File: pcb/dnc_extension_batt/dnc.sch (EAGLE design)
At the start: 105 parts, among them Q1 IRF9321PBF, Q2 IRF9321PBF, Q3 BSS138, Q5 BSS138, U1 LCD-16X2NOHOLES, U2 74HCT595D

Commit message: minor change : - logo size - add fuse on led - enclosure
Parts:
- U$2, U$6MOV: value LOGO -> LOGOSIZE2; device pierre_vv:LOGO -> pierre_vv:LOGOSIZE2
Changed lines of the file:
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@@
 <grid distance="0.1" unitdist="inch" unit="inch" style="lines" multiple="1" display="no" altdistance="0.01" altunitdist="inch" altunit="inch"/>
 <layers>
-<layer number="1" name="Top" color="4" fill="1" visible="no" active="no"/>
-<layer number="16" name="Bottom" color="1" fill="1" visible="no" active="no"/>
-<layer number="17" name="Pads" color="2" fill="1" visible="no" active="no"/>
-<layer number="18" name="Vias" color="2" fill="1" visible="no" active="no"/>
-<layer number="19" name="Unrouted" color="13" fill="1" visible="no" active="no"/>
-<layer number="20" name="Dimension" color="15" fill="1" visible="no" active="no"/>
-<layer number="21" name="tPlace" color="7" fill="1" visible="no" active="no"/>
-<layer number="22" name="bPlace" color="7" fill="1" visible="no" active="no"/>
-<layer number="23" name="tOrigins" color="15" fill="1" visible="no" active="no"/>
-<layer number="24" name="bOrigins" color="15" fill="1" visible="no" active="no"/>
-<layer number="25" name="tNames" color="7" fill="1" visible="no" active="no"/>
-<layer number="26" name="bNames" color="7" fill="1" visible="no" active="no"/>
-<layer number="27" name="tValues" color="7" fill="1" visible="no" active="no"/>
-<layer number="28" name="bValues" color="7" fill="1" visible="no" active="no"/>
+<layer number="1" name="Top" color="4" fill="1" visible="yes" active="no"/>
+<layer number="16" name="Bottom" color="1" fill="1" visible="yes" active="no"/>
+<layer number="17" name="Pads" color="2" fill="1" visible="yes" active="no"/>
+<layer number="18" name="Vias" color="2" fill="1" visible="yes" active="no"/>
+<layer number="19" name="Unrouted" color="13" fill="1" visible="yes" active="no"/>
+<layer number="20" name="Dimension" color="15" fill="1" visible="yes" active="no"/>
+<layer number="21" name="tPlace" color="7" fill="1" visible="yes" active="no"/>
+<layer number="22" name="bPlace" color="7" fill="1" visible="yes" active="no"/>
+<layer number="23" name="tOrigins" color="15" fill="1" visible="yes" active="no"/>
+<layer number="24" name="bOrigins" color="15" fill="1" visible="yes" active="no"/>
+<layer number="25" name="tNames" color="7" fill="1" visible="yes" active="no"/>
+<layer number="26" name="bNames" color="7" fill="1" visible="yes" active="no"/>
+<layer number="27" name="tValues" color="7" fill="1" visible="yes" active="no"/>
+<layer number="28" name="bValues" color="7" fill="1" visible="yes" active="no"/>
 <layer number="29" name="tStop" color="7" fill="3" visible="no" active="no"/>
 <layer number="30" name="bStop" color="7" fill="6" visible="no" active="no"/>
@@
 <layer number="35" name="tGlue" color="7" fill="4" visible="no" active="no"/>
 <layer number="36" name="bGlue" color="7" fill="5" visible="no" active="no"/>
-<layer number="37" name="tTest" color="7" fill="1" visible="no" active="no"/>
-<layer number="38" name="bTest" color="7" fill="1" visible="no" active="no"/>
+<layer number="37" name="tTest" color="7" fill="1" visible="yes" active="no"/>
+<layer number="38" name="bTest" color="7" fill="1" visible="yes" active="no"/>
 <layer number="39" name="tKeepout" color="4" fill="11" visible="no" active="no"/>
 <layer number="40" name="bKeepout" color="1" fill="11" visible="no" active="no"/>
@@
 <layer number="44" name="Drills" color="7" fill="1" visible="no" active="no"/>
 <layer number="45" name="Holes" color="7" fill="1" visible="no" active="no"/>
-<layer number="46" name="Milling" color="3" fill="1" visible="no" active="no"/>
-<layer number="47" name="Measures" color="7" fill="1" visible="no" active="no"/>
-<layer number="48" name="Document" color="7" fill="1" visible="no" active="no"/>
-<layer number="49" name="Reference" color="7" fill="1" visible="no" active="no"/>
-<layer number="50" name="dxf" color="7" fill="1" visible="no" active="no"/>
-<layer number="51" name="tDocu" color="14" fill="1" visible="no" active="no"/>
-<layer number="52" name="bDocu" color="14" fill="1" visible="no" active="no"/>
-<layer number="53" name="tGND_GNDA" color="7" fill="9" visible="no" active="no"/>
-<layer number="54" name="bGND_GNDA" color="1" fill="9" visible="no" active="no"/>
-<layer number="56" name="wert" color="7" fill="1" visible="no" active="no"/>
-<layer number="57" name="tCAD" color="7" fill="1" visible="no" active="no"/>
+<layer number="46" name="Milling" color="3" fill="1" visible="yes" active="no"/>
+<layer number="47" name="Measures" color="7" fill="1" visible="yes" active="no"/>
+<layer number="48" name="Document" color="7" fill="1" visible="yes" active="no"/>
+<layer number="49" name="Reference" color="7" fill="1" visible="yes" active="no"/>
+<layer number="50" name="dxf" color="7" fill="1" visible="yes" active="no"/>
+<layer number="51" name="tDocu" color="14" fill="1" visible="yes" active="no"/>
+<layer number="52" name="bDocu" color="14" fill="1" visible="yes" active="no"/>
+<layer number="53" name="tGND_GNDA" color="7" fill="9" visible="yes" active="no"/>
+<layer number="54" name="bGND_GNDA" color="1" fill="9" visible="yes" active="no"/>
+<layer number="56" name="wert" color="7" fill="1" visible="yes" active="no"/>
+<layer number="57" name="tCAD" color="7" fill="1" visible="yes" active="no"/>
 <layer number="90" name="Modules" color="5" fill="1" visible="yes" active="yes"/>
 <layer number="91" name="Nets" color="2" fill="1" visible="yes" active="yes"/>
@@
 </part>
 <part name="GND13" library="SparkFun-Aesthetics" deviceset="GND" device=""/>
-<part name="U$2" library="pierre_vv" deviceset="LOGO" device=""/>
+<part name="U$2" library="pierre_vv" deviceset="LOGO" device="SIZE2" value="LOGOSIZE2"/>
 <part name="GND22" library="SparkFun-Aesthetics" deviceset="GND" device=""/>
 <part name="RAW_IN" library="pierre_vv" deviceset="DNC_IN2" device="PWR" value="SUPPLY">
@@
 </part>
 <part name="U$5" library="pierre_vv" deviceset="BOITIER" device="BOITIER_FARNELLE_479-0020-0"/>
-<part name="U$6MOV" library="pierre_vv" deviceset="LOGO" device=""/>
+<part name="U$6MOV" library="pierre_vv" deviceset="LOGO" device="SIZE2" value="LOGOSIZE2"/>
 <part name="U1" library="SparkFun-Displays" deviceset="LCD-16X2" device="NOHOLES"/>
 <part name="GND6" library="SparkFun-Aesthetics" deviceset="GND" device=""/>

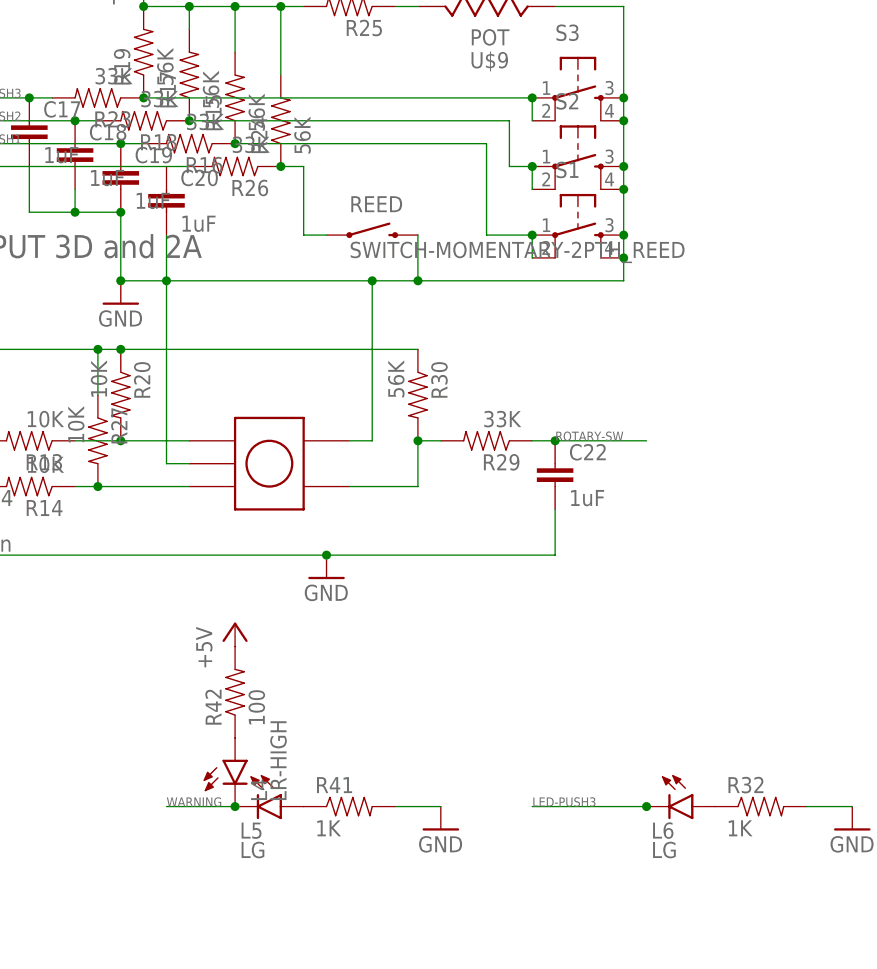
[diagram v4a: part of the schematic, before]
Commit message: change minor : - add rj45 for led string - add select pam led or flex
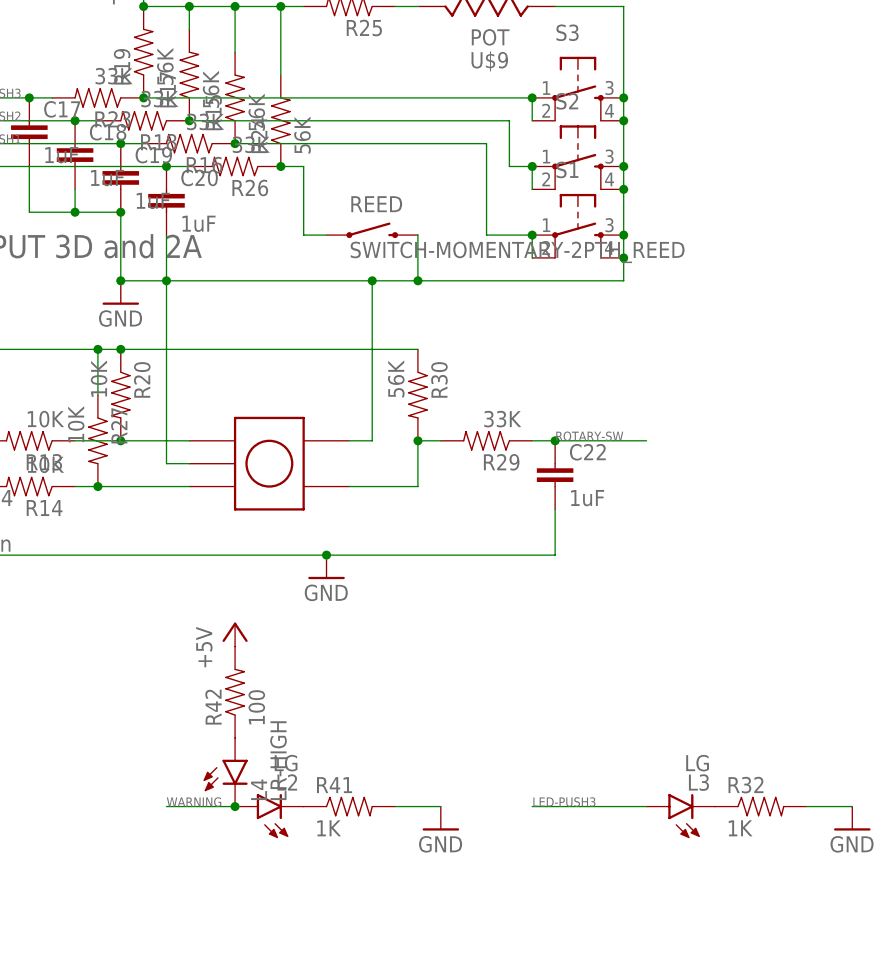
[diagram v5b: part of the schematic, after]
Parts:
- removed L5, L6: LG, SparkFun-LED:LED1206
- added L2, L3: LG, SparkFun-LED:LED1206
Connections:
- net LED-PUSH3: now also L3.A; no longer L6.C
- net N$30: now also L2.C; no longer L5.A
- net N$35: now also L3.C; no longer L6.A
- net WARNING: now also L2.A; no longer L5.C
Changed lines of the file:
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@@
 <grid distance="0.1" unitdist="inch" unit="inch" style="lines" multiple="1" display="no" altdistance="0.01" altunitdist="inch" altunit="inch"/>
 <layers>
-<layer number="1" name="Top" color="4" fill="1" visible="yes" active="no"/>
-<layer number="16" name="Bottom" color="1" fill="1" visible="yes" active="no"/>
-<layer number="17" name="Pads" color="2" fill="1" visible="yes" active="no"/>
-<layer number="18" name="Vias" color="2" fill="1" visible="yes" active="no"/>
-<layer number="19" name="Unrouted" color="13" fill="1" visible="yes" active="no"/>
-<layer number="20" name="Dimension" color="15" fill="1" visible="yes" active="no"/>
-<layer number="21" name="tPlace" color="7" fill="1" visible="yes" active="no"/>
-<layer number="22" name="bPlace" color="7" fill="1" visible="yes" active="no"/>
-<layer number="23" name="tOrigins" color="15" fill="1" visible="yes" active="no"/>
-<layer number="24" name="bOrigins" color="15" fill="1" visible="yes" active="no"/>
-<layer number="25" name="tNames" color="7" fill="1" visible="yes" active="no"/>
-<layer number="26" name="bNames" color="7" fill="1" visible="yes" active="no"/>
-<layer number="27" name="tValues" color="7" fill="1" visible="yes" active="no"/>
-<layer number="28" name="bValues" color="7" fill="1" visible="yes" active="no"/>
+<layer number="1" name="Top" color="4" fill="1" visible="no" active="no"/>
+<layer number="16" name="Bottom" color="1" fill="1" visible="no" active="no"/>
+<layer number="17" name="Pads" color="2" fill="1" visible="no" active="no"/>
+<layer number="18" name="Vias" color="2" fill="1" visible="no" active="no"/>
+<layer number="19" name="Unrouted" color="13" fill="1" visible="no" active="no"/>
+<layer number="20" name="Dimension" color="15" fill="1" visible="no" active="no"/>
+<layer number="21" name="tPlace" color="7" fill="1" visible="no" active="no"/>
+<layer number="22" name="bPlace" color="7" fill="1" visible="no" active="no"/>
+<layer number="23" name="tOrigins" color="15" fill="1" visible="no" active="no"/>
+<layer number="24" name="bOrigins" color="15" fill="1" visible="no" active="no"/>
+<layer number="25" name="tNames" color="7" fill="1" visible="no" active="no"/>
+<layer number="26" name="bNames" color="7" fill="1" visible="no" active="no"/>
+<layer number="27" name="tValues" color="7" fill="1" visible="no" active="no"/>
+<layer number="28" name="bValues" color="7" fill="1" visible="no" active="no"/>
 <layer number="29" name="tStop" color="7" fill="3" visible="no" active="no"/>
 <layer number="30" name="bStop" color="7" fill="6" visible="no" active="no"/>
@@
 <layer number="35" name="tGlue" color="7" fill="4" visible="no" active="no"/>
 <layer number="36" name="bGlue" color="7" fill="5" visible="no" active="no"/>
-<layer number="37" name="tTest" color="7" fill="1" visible="yes" active="no"/>
-<layer number="38" name="bTest" color="7" fill="1" visible="yes" active="no"/>
+<layer number="37" name="tTest" color="7" fill="1" visible="no" active="no"/>
+<layer number="38" name="bTest" color="7" fill="1" visible="no" active="no"/>
 <layer number="39" name="tKeepout" color="4" fill="11" visible="no" active="no"/>
 <layer number="40" name="bKeepout" color="1" fill="11" visible="no" active="no"/>
@@
 <layer number="44" name="Drills" color="7" fill="1" visible="no" active="no"/>
 <layer number="45" name="Holes" color="7" fill="1" visible="no" active="no"/>
-<layer number="46" name="Milling" color="3" fill="1" visible="yes" active="no"/>
-<layer number="47" name="Measures" color="7" fill="1" visible="yes" active="no"/>
-<layer number="48" name="Document" color="7" fill="1" visible="yes" active="no"/>
-<layer number="49" name="Reference" color="7" fill="1" visible="yes" active="no"/>
-<layer number="50" name="dxf" color="7" fill="1" visible="yes" active="no"/>
-<layer number="51" name="tDocu" color="14" fill="1" visible="yes" active="no"/>
-<layer number="52" name="bDocu" color="14" fill="1" visible="yes" active="no"/>
-<layer number="53" name="tGND_GNDA" color="7" fill="9" visible="yes" active="no"/>
-<layer number="54" name="bGND_GNDA" color="1" fill="9" visible="yes" active="no"/>
-<layer number="56" name="wert" color="7" fill="1" visible="yes" active="no"/>
-<layer number="57" name="tCAD" color="7" fill="1" visible="yes" active="no"/>
+<layer number="46" name="Milling" color="3" fill="1" visible="no" active="no"/>
+<layer number="47" name="Measures" color="7" fill="1" visible="no" active="no"/>
+<layer number="48" name="Document" color="7" fill="1" visible="no" active="no"/>
+<layer number="49" name="Reference" color="7" fill="1" visible="no" active="no"/>
+<layer number="50" name="dxf" color="7" fill="1" visible="no" active="no"/>
+<layer number="51" name="tDocu" color="14" fill="1" visible="no" active="no"/>
+<layer number="52" name="bDocu" color="14" fill="1" visible="no" active="no"/>
+<layer number="53" name="tGND_GNDA" color="7" fill="9" visible="no" active="no"/>
+<layer number="54" name="bGND_GNDA" color="1" fill="9" visible="no" active="no"/>
+<layer number="56" name="wert" color="7" fill="1" visible="no" active="no"/>
+<layer number="57" name="tCAD" color="7" fill="1" visible="no" active="no"/>
 <layer number="90" name="Modules" color="5" fill="1" visible="yes" active="yes"/>
 <layer number="91" name="Nets" color="2" fill="1" visible="yes" active="yes"/>
@@
 <part name="R42" library="SparkFun-Passives" deviceset="RESISTOR" device="0603-RES" value="100"/>
 <part name="P+8" library="supply1" deviceset="+5V" device=""/>
-<part name="L5" library="SparkFun-LED" deviceset="LED" device="1206" value="LG"/>
 <part name="R41" library="SparkFun-Passives" deviceset="RESISTOR" device="0603-RES" value="1K"/>
 <part name="GND9" library="SparkFun" deviceset="GND" device=""/>
@@
 <attribute name="P" value="250mw"/>
 </part>
-<part name="L6" library="SparkFun-LED" deviceset="LED" device="1206" value="LG"/>
 <part name="R32" library="SparkFun-Passives" deviceset="RESISTOR" device="0603-RES" value="1K"/>
 <part name="GND15" library="SparkFun" deviceset="GND" device=""/>
@@
 <part name="JP3" library="SparkFun" deviceset="FIDUCIAL" device="1X2.5"/>
 <part name="JP4" library="SparkFun" deviceset="FIDUCIAL" device="1X2.5"/>
+<part name="L2" library="SparkFun-LED" deviceset="LED" device="1206" value="LG"/>
+<part name="L3" library="SparkFun-LED" deviceset="LED" device="1206" value="LG"/>
 </parts>
 <sheets>
@@
 <instance part="R42" gate="G$1" x="53.34" y="35.56" rot="R90"/>
 <instance part="P+8" gate="1" x="53.34" y="43.18"/>
-<instance part="L5" gate="G$1" x="58.42" y="22.86" rot="R270"/>
 <instance part="R41" gate="G$1" x="66.04" y="22.86"/>
 <instance part="GND9" gate="1" x="76.2" y="20.32"/>
@@
 <attribute name="P" x="358.14" y="180.34" size="1.778" layer="96" rot="R90" display="off"/>
 </instance>
-<instance part="L6" gate="G$1" x="104.14" y="22.86" rot="R270"/>
 <instance part="R32" gate="G$1" x="111.76" y="22.86"/>
 <instance part="GND15" gate="1" x="121.92" y="20.32"/>
@@
 <instance part="JP3" gate="G$1" x="294.64" y="12.7"/>
 <instance part="JP4" gate="G$1" x="299.72" y="12.7"/>
+<instance part="L2" gate="G$1" x="55.88" y="22.86" rot="R90"/>
+<instance part="L3" gate="G$1" x="101.6" y="22.86" rot="R90"/>
 </instances>
 <busses>
@@
 <wire x1="45.72" y1="93.98" x2="22.86" y2="93.98" width="0.1524" layer="91"/>
 <label x="22.86" y="93.98" size="1.016" layer="95"/>
+<junction x="45.72" y="93.98"/>
 </segment>
 <segment>
@@
 <pinref part="L4" gate="G$1" pin="A"/>
 <pinref part="R42" gate="G$1" pin="1"/>
-</segment>
-</net>
-<net name="N$30" class="0">
-<segment>
-<pinref part="L5" gate="G$1" pin="A"/>
-<pinref part="R41" gate="G$1" pin="1"/>
 </segment>
 </net>
@@
 <wire x1="45.72" y1="22.86" x2="53.34" y2="22.86" width="0.1524" layer="91"/>
 <label x="45.72" y="22.86" size="1.016" layer="95"/>
-<pinref part="L5" gate="G$1" pin="C"/>
 <pinref part="L4" gate="G$1" pin="C"/>
+<pinref part="L2" gate="G$1" pin="A"/>
 <junction x="53.34" y="22.86"/>
 </segment>
@@
 <wire x1="86.36" y1="22.86" x2="99.06" y2="22.86" width="0.1524" layer="91"/>
 <label x="86.36" y="22.86" size="1.016" layer="95"/>
-<pinref part="L6" gate="G$1" pin="C"/>
-<junction x="99.06" y="22.86"/>
+<pinref part="L3" gate="G$1" pin="A"/>
 </segment>
 <segment>
@@
 <wire x1="205.74" y1="124.46" x2="215.9" y2="124.46" width="0.1524" layer="91"/>
 <label x="208.28" y="124.46" size="1.016" layer="95"/>
-</segment>
-</net>
-<net name="N$35" class="0">
-<segment>
-<pinref part="L6" gate="G$1" pin="A"/>
-<pinref part="R32" gate="G$1" pin="1"/>
 </segment>
 </net>
@@
 </segment>
 </net>
+<net name="N$30" class="0">
+<segment>
+<pinref part="R41" gate="G$1" pin="1"/>
+<pinref part="L2" gate="G$1" pin="C"/>
+</segment>
+</net>
+<net name="N$35" class="0">
+<segment>
+<pinref part="R32" gate="G$1" pin="1"/>
+<pinref part="L3" gate="G$1" pin="C"/>
+</segment>
+</net>
